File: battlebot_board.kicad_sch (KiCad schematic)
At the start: 40 parts, among them J1 Conn_01x02_Pin, J2 Conn_01x04_Pin, J3 JST_SMD_1.0mm_Vertical, J5 JST_02, J6 JST_02, Q1 AO3400A, Q2 AO3400A, SW1 Switch_Tactile_CnK, U1 AP63203WU, U2 LPC824M201JHI33, U3 TMP102, U4 LSM6DSOX, U5 W25Q128JVP

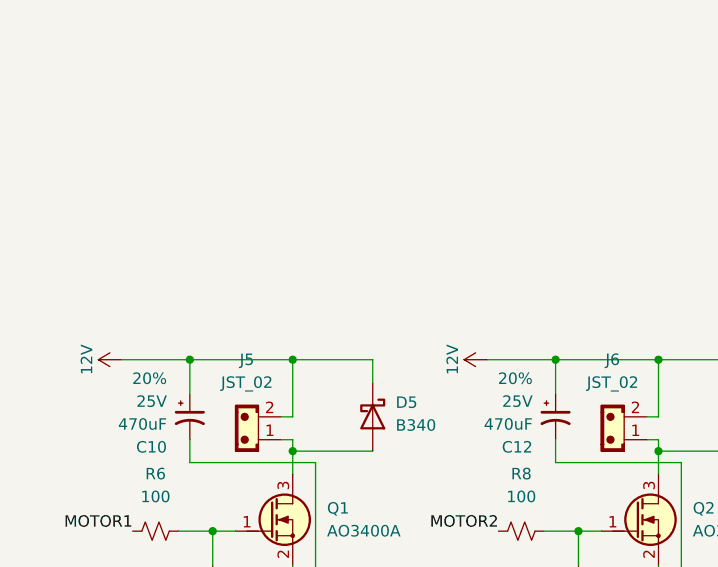
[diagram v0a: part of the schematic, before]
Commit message: added fuses and moved diodes for thermal protection
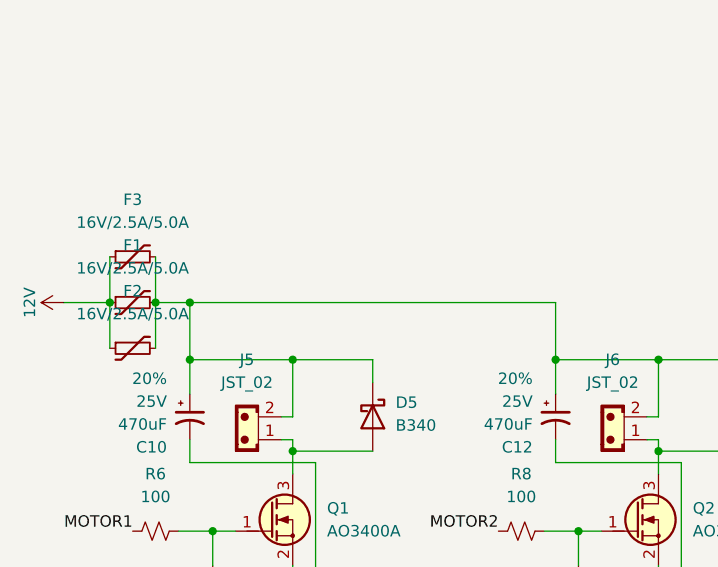
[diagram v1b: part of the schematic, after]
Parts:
- added F1, F2, F3: 16V/2.5A/5.0A, PCM_SparkFun-Fuse:1812, symbol PCM_SparkFun-Fuse:Fuse 16V/2.5A/5.0A
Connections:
- net 12V: now also F1.1, F2.1, F3.1; no longer C10.1, C12.1, D4.1 (K), D5.1 (K), J5.2, J6.2
- new net: C10.1, C12.1, D4.1 (K), D5.1 (K), F1.2, F2.2, F3.2, J5.2, J6.2

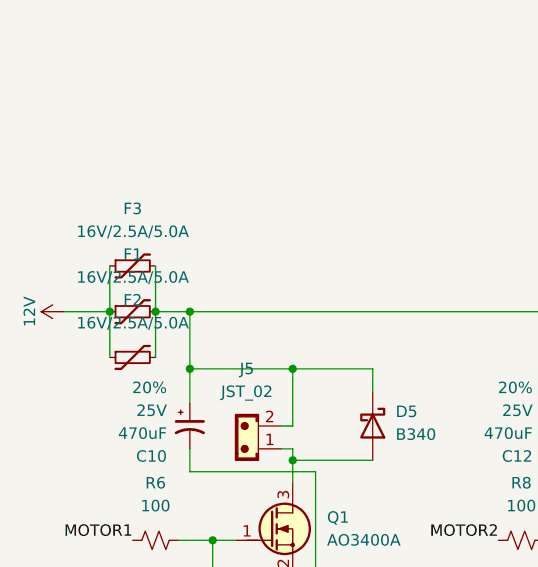
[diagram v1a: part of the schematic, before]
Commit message: replaced parallel fuses with fuse blade holder
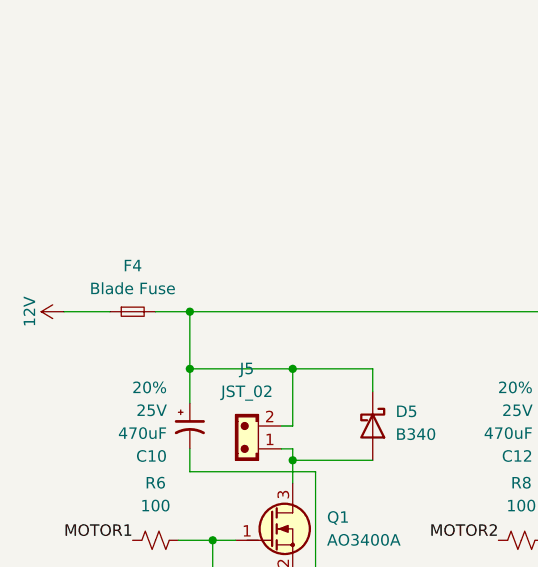
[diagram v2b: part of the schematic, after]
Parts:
- removed F1, F2, F3: 16V/2.5A/5.0A, PCM_SparkFun-Fuse:1812, symbol PCM_SparkFun-Fuse:Fuse 16V/2.5A/5.0A
- added F4: Blade Fuse, PCM_SparkFun-Fuse:Fuseholder_Automotive, symbol PCM_SparkFun-Fuse:Fuse_Holder-Blade
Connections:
- net 12V: now also F4.1
- net at C10.1, C12.1, D4.1 (K)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: now also F4.2

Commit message: expose I2C1, fix power delivery wiring, and change credits
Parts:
- added J4, J7: Conn_01x02, Connector_JST:JST_EH_B2B-EH-A_1x02_P2.50mm_Vertical, symbol PCM_4ms_Connector:Conn_01x02
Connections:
- net 3.3V: now also J7.1 (Pin_1)
- net GND: now also J7.2 (Pin_2)
- net SCL1: now also J4.2 (Pin_2)
- net SDA1: now also J4.1 (Pin_1)

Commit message: logos and housekeeping
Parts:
- removed J7: Conn_01x02, Connector_JST:JST_EH_B2B-EH-A_1x02_P2.50mm_Vertical, symbol PCM_4ms_Connector:Conn_01x02

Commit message: redesign
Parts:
- removed C1, C2: 10uF, PCM_SparkFun-Capacitor:C_0402_1005Metric, symbol PCM_SparkFun-Capacitor:10uF_0402_6.3V_20%
- removed C10: 470uF, PCM_SparkFun-Capacitor:Electrolytic_10.3x10.3mm, symbol PCM_SparkFun-Capacitor:470uF_10x10_25V_20%
- removed C3, C7, C8: 0.1uF, PCM_SparkFun-Capacitor:C_0402_1005Metric, symbol PCM_SparkFun-Capacitor:0.1uF_0402_16V_10%
- removed C5: 22uF, PCM_SparkFun-Capacitor:C_0603_1608Metric, symbol PCM_SparkFun-Capacitor:22uF_0603_6.3V_20%
- removed D3: Green, PCM_SparkFun-LED:LED_0603_1608Metric_Green, symbol PCM_SparkFun-LED:LED_Green_0603
- removed D4, D5: B340, Diode_SMD:D_SMC, symbol Diode:B340
- removed F4: Blade Fuse, PCM_SparkFun-Fuse:Fuseholder_Automotive, symbol PCM_SparkFun-Fuse:Fuse_Holder-Blade
- removed H1, H2, H3, H4: (no value), PCM_fab:MountingHole_M2, symbol PCM_fab:MountingHole_M2
- removed J1: Conn_01x02_Pin, Connector_JST:JST_EH_B2B-EH-A_1x02_P2.50mm_Vertical, symbol Connector:Conn_01x02_Pin
- removed J2: Conn_01x04_Pin, Connector_JST:JST_EH_B4B-EH-A_1x04_P2.50mm_Vertical, symbol Connector:Conn_01x04_Pin
- removed J3: JST_SMD_1.0mm_Vertical, PCM_SparkFun-Connector:JST_1x04_P1.0mm_Vertical_SMD, symbol PCM_SparkFun-Connector:Conn_01x04_JST_P1.0mm_Vertical_SMD
- removed J4: Conn_01x02, Connector_JST:JST_EH_B2B-EH-A_1x02_P2.50mm_Vertical, symbol PCM_4ms_Connector:Conn_01x02
- removed J5, J6: JST_02, Connector_JST:JST_EH_B2B-EH-A_1x02_P2.50mm_Vertical, symbol PCM_SL_Connectors:JST_02
- removed Q1, Q2: AO3400A, Package_TO_SOT_SMD:SOT-23, symbol PCM_Transistor_MOSFET_AKL:AO3400A
- removed R10, R7, R9: 10k, PCM_SparkFun-Resistor:R_0402_1005Metric, symbol PCM_SparkFun-Resistor:10k_0402
- removed R4, R5: 4.7k, PCM_SparkFun-Resistor:R_0402_1005Metric, symbol PCM_SparkFun-Resistor:4.7k_0402
- removed R6, R8: 100, PCM_SparkFun-Resistor:R_0402_1005Metric, symbol PCM_SparkFun-Resistor:100_0402
- removed SW1: Switch_Tactile_CnK, PCM_fab:Button_CnK_PTS636.0_6x3.5mm, symbol PCM_fab:Switch_Tactile_CnK
- removed U2: LPC824M201JHI33, Package_DFN_QFN:QFN-32-1EP_5x5mm_P0.5mm_EP3.45x3.45mm, symbol MCU_NXP_LPC:LPC824M201JHI33
- removed U3: TMP102, PCM_SparkFun-Semiconductor-Standard:SOT-563, symbol PCM_SparkFun-Sensor:TMP102
- removed U4: LSM6DSOX, PCM_SparkFun-Sensor:ST_LGA-14L_2.5x3.0mm_P0.5mm_4x3, symbol PCM_SparkFun-Sensor:LSM6DSOX
- removed U5: W25Q128JVP, Package_SON:WSON-8-1EP_6x5mm_P1.27mm_EP3.4x4.3mm, symbol Memory_Flash:W25Q128JVP
- added C1, C10, C11, C14, C2, C5, C6: 0.1uF, PCM_SparkFun-Capacitor:C_0402_1005Metric, symbol PCM_SparkFun-Capacitor:0.1uF_0402_16V_10%
- added C13: 470uF, PCM_SparkFun-Capacitor:Electrolytic_10.3x10.3mm, symbol PCM_SparkFun-Capacitor:470uF_10x10_25V_20%
- added C15, C8: 1.0uF, PCM_SparkFun-Capacitor:C_0402_1005Metric, symbol PCM_SparkFun-Capacitor:1.0uF_0402_16V_10%
- added C3: 22uF, PCM_SparkFun-Capacitor:C_0603_1608Metric, symbol PCM_SparkFun-Capacitor:22uF_0603_6.3V_20%
- added C7: 10uF, PCM_SparkFun-Capacitor:C_0402_1005Metric, symbol PCM_SparkFun-Capacitor:10uF_0402_6.3V_20%
- added C9: 10nF, PCM_SparkFun-Capacitor:C_0402_1005Metric, symbol PCM_SparkFun-Capacitor:10nF_0402_25V_10%
- added D1: Green, PCM_SparkFun-LED:LED_0603_1608Metric_Green, symbol PCM_SparkFun-LED:LED_Green_0603
- added D2: PMEG4005EJ, Diode_SMD:D_SOD-323F, symbol Diode:PMEG4005EJ
- added F1: 16V/2.5A/5.0A, PCM_SparkFun-Fuse:1812, symbol PCM_SparkFun-Fuse:Fuse 16V/2.5A/5.0A
- added J1, J3: Conn_01x03_Socket, PCM_SparkFun-Connector:JST_1x03_P1.0mm_Vertical_SMD, symbol Connector:Conn_01x03_Socket
- added J2: Barrel_Jack_SMD, PCM_SparkFun-Connector:Barrel_Jack_SMD, symbol PCM_SparkFun-Connector:Barrel_Jack_SMD
- added J4: Conn_01x04_Pin, Connector_PinHeader_1.27mm:PinHeader_1x04_P1.27mm_Vertical, symbol Connector:Conn_01x04_Pin
- added J5: Conn_01x04_Socket, PCM_SparkFun-Connector:JST_1x04_P1.0mm_Vertical_SMD, symbol Connector:Conn_01x04_Socket
- added J6: Conn_01x02_Pin, Connector_PinHeader_1.27mm:PinHeader_1x02_P1.27mm_Vertical, symbol Connector:Conn_01x02_Pin
- added J7: Conn_02x03, Connector_PinHeader_1.27mm:PinHeader_2x03_P1.27mm_Vertical, symbol PCM_4ms_Connector:Conn_02x03
- added L2: 600 Ohm, PCM_SparkFun-Capacitor:C_0805_2012Metric, symbol PCM_SparkFun-Coil:Ferrite_600Ohm_0805_500mA
- added L3: 10uH, PCM_SparkFun-Capacitor:C_0805_2012Metric, symbol PCM_SparkFun-Coil:10uH_0805_0.35A
- added R4, R5: 100k, PCM_SparkFun-Resistor:R_0402_1005Metric, symbol PCM_SparkFun-Resistor:100k_0402
- added R6: 33k, PCM_SparkFun-Resistor:R_0402_1005Metric, symbol PCM_SparkFun-Resistor:33k_0402
- added U2: LSM6DSOX, PCM_SparkFun-Sensor:ST_LGA-14L_2.5x3.0mm_P0.5mm_4x3, symbol PCM_SparkFun-Sensor:LSM6DSOX
- added U3: W25Q128JVP, Package_SON:WSON-8-1EP_6x5mm_P1.27mm_EP3.4x4.3mm, symbol Memory_Flash:W25Q128JVP
- added U4: STM32G4A1KEUx, Package_DFN_QFN:QFN-32-1EP_5x5mm_P0.5mm_EP3.45x3.45mm, symbol MCU_ST_STM32G4:STM32G4A1KEUx
- added U5: AP3012, PCM_SparkFun-Semiconductor-Standard:SOT23-5, symbol PCM_SparkFun-IC-Power:AP3012
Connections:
- net 12V is gone; now on net VIN: U1.3 (IN)
- net CS1 is gone; now on net GND: R2.1
- net 3.3V: now also C11.1, C14.1, C3.1, C5.1, C6.1, C7.1, J4.1 (Pin_1), J6.1 (Pin_1), L2.2, L3.1, R4.2, U2.5 (VDDIO), U2.8 (VDD), U3.3 (~{WP}/IO_{2}), U3.7 (~{HOLD}/~{RESET}/IO_{3}), U3.8 (VCC), U4.1 (VDD), U4.17 (VDD), U5.5 (IN); no longer R2.2
- net CS2: now also U3.1 (~{CS}), U4.25 (PA15)
- net GND: now also C1.2, C10.2, C11.2, C13.2, C14.2, C15.2, C3.2, C5.2, C6.2, C7.2, C8.2, C9.2, D1.1 (K), J1.3 (Pin_3), J2.GND, J3.3 (Pin_3), J4.4 (Pin_4), J5.4 (Pin_4), J7.2 (+12V), J7.4 (GND), J7.6 (GND), R6.1, U2.6 (GND), U2.7 (GND), U3.4 (GND), U4.14 (VSSA), U4.16 (VSS), U4.32 (VSS), U4.33 (VSS), U5.2 (GND)
- net MISO2: now also U3.2 (DO/IO_{1}), U4.27 (PB4)
- net MOSI2: now also U3.5 (DI/IO_{0}), U4.28 (PB5)
- net NRST: now also C10.1, U4.4 (PG10)
- net SCK2: now also U3.6 (CLK), U4.26 (PB3)
- net SWCLK: now also J4.3 (Pin_3), U4.24 (PA14)
- net SWDIO: now also J4.2 (Pin_2), U4.23 (PA13)
- net VIN: now reaches C12.1
- net VIN: now also U1.2 (EN), C1.1, C13.1, F1.2, J1.2 (Pin_2), J3.2 (Pin_2)
- net at L1.1, U1.5 (SW): now also C2.2
- net at U1.6 (BST): now also C2.1
- new net: R4.1, U5.4 (~{SHDN})
- new net: C8.1, C9.1, L2.1, U4.15 (VDDA)
- new net: F1.1, J2.PWR
- new net: R5.1, R6.2, U5.3 (FB)
- new net: D1.2 (A), J6.2 (Pin_2)
- new net: D2.2 (A), L3.2, U5.1 (SW)
- new net 5V: C15.1, D2.1 (K), J5.3 (Pin_3), J7.1 (+12V), J7.3 (GND), J7.5 (GND), R5.2
- new net BOOT0: R2.2, U4.31 (PB8)
- new net CH1: J1.1 (Pin_1), U4.18 (PA8)
- new net CH2: J3.1 (Pin_1), U4.19 (PA9)
- new net CS: U2.12 (~{CS}), U4.9 (PA4)
- new net MISO: U2.1 (SDO/SA0), U4.11 (PA6)
- new net MOSI: U2.14 (SDA), U4.12 (PA7)
- new net RX2: J5.2 (Pin_2), U4.8 (PA3)
- new net SCK: U2.13 (SCL), U4.10 (PA5)
- new net TX2: J5.1 (Pin_1), U4.7 (PA2)

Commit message: redesign udpate
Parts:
- added C16, C17: 0.1uF, PCM_SparkFun-Capacitor:C_0402_1005Metric, symbol PCM_SparkFun-Capacitor:0.1uF_0402_16V_10%
- added F2, F3: 6V/0.5A/1A, PCM_SparkFun-Fuse:0805, symbol PCM_SparkFun-Fuse:Fuse 6V/0.5A/1A
- added J8: Socket_01x02, Connector_PinHeader_1.27mm:PinHeader_1x02_P1.27mm_Vertical, symbol PCM_4ms_Connector:Socket_01x02
- added J9: Conn_01x02_Pin, Connector_PinHeader_1.27mm:PinHeader_1x02_P1.27mm_Vertical, symbol Connector:Conn_01x02_Pin
- added R7, R9: 10, PCM_SparkFun-Resistor:R_0402_1005Metric, symbol PCM_SparkFun-Resistor:10_0402
- added R8: 100, PCM_SparkFun-Resistor:R_0402_1005Metric, symbol PCM_SparkFun-Resistor:100_0402
- added U6: MCP2562-E-MF, Package_DFN_QFN:DFN-8-1EP_3x3mm_P0.65mm_EP1.55x2.4mm, symbol Interface_CAN_LIN:MCP2562-E-MF
- added U7: BD1020HFV, Package_TO_SOT_SMD:HVSOF5, symbol Sensor_Temperature:BD1020HFV
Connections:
- net 3.3V: now also C17.2, U6.5 (Vio)
- net 5V: now also C16.2, F2.1, U6.3 (VDD), U7.4 (VDD); no longer J7.1 (+12V), J7.3 (GND), J7.5 (GND)
- net GND: now also C16.1, C17.1, U6.2 (VSS), U6.8 (SHDN), U7.2 (PG), U7.5 (GND)
- net VIN: now also F3.2; no longer C1.1, U1.2 (EN), U1.3 (IN)
- net CAN_RX: now reaches U4.21 (PA11)
- net CAN_RX: now also U6.4 (RXD)
- net CAN_TX: now reaches U4.22 (PA12)
- net CAN_TX: now also U6.1 (TXD)
- net ADC: now reaches U4.5 (PA0)
- net ADC: now also U7.3 (OUT)
- new net: R7.1, R9.2
- new net: R7.2, R8.1
- new net: J9.1 (Pin_1), R9.1, U6.7 (CANH)
- new net: J8.2 (Pin_2), J9.2 (Pin_2), U6.6 (CANL)
- new net: F2.2, J7.1 (+12V), J7.3 (GND), J7.5 (GND)
- new net: J8.1 (Pin_1), R8.2
- new net: C1.1, F3.1, U1.2 (EN), U1.3 (IN)
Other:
- moved on the sheet: F1
